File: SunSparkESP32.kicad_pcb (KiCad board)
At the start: 4 copper layers, 38.1 x 58.2 mm, 50 parts, among them J1 Conn_01x02_Pin, J2 USB_C_Receptacle_USB2.0, J4 Conn_01x15_Pin, J5 Conn_01x03_Pin, J6 Conn_01x15_Pin, J7 Conn_01x01_Pin, Q1 IRLML6244TRPBF, Q2 IRLML6244TRPBF, SW1 SW_Push, SW2 SW_Push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

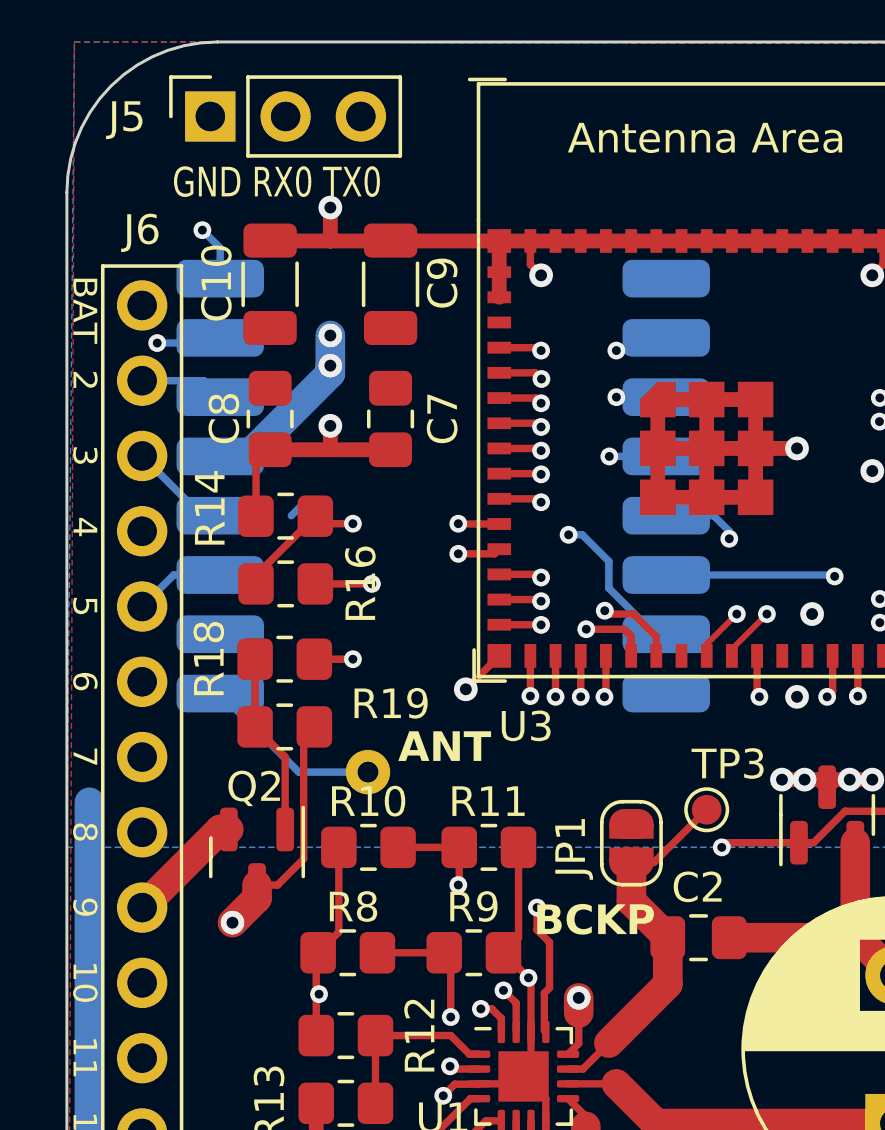
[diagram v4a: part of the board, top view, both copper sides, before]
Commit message: Final adjustments for release preparation -Updated schematics, BOM and fabrication files -Added solder jumper so RFM96 can be powered independently
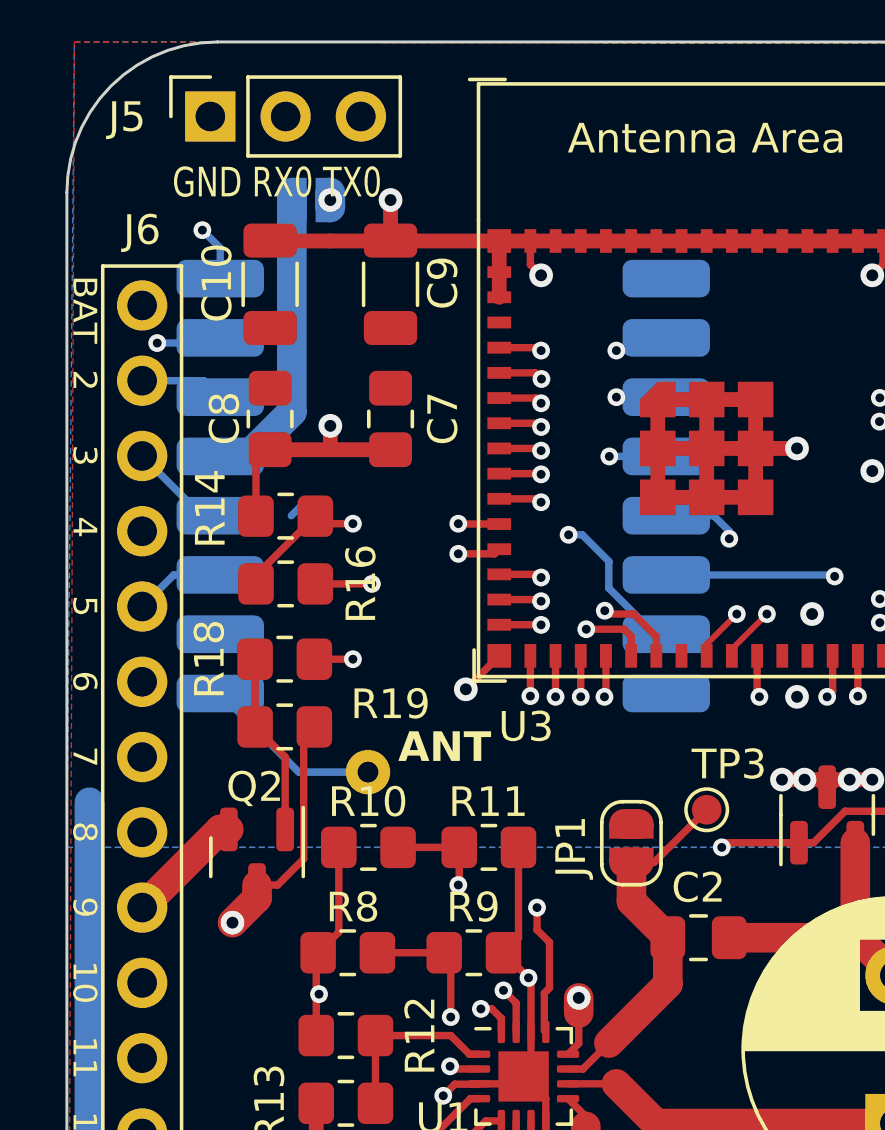
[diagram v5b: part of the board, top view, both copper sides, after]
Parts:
- added JP2: SolderJumper_2_Open, Jumper:SolderJumper-2_P1.3mm_Open_RoundedPad1.0x1.5mm, B.Cu at (60.3, 44.7)
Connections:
- U4 pad 13: +BATT -> Net-(JP2-A)
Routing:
- net Net-(JP2-A): track 0.00 -> 10.2 mm
- net +BATT: track 13.3 -> 7.10 mm, vias 6 -> 5
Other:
- board text removed: "BCKP"
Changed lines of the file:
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@@
   (net 64 "R_DIV_SUPPLY")
   (net 65 "Net-(U1-BAT)")
+  (net 66 "Net-(JP2-A)")
   (footprint "Capacitor_SMD:C_0805_2012Metric_Pad1.18x1.45mm_HandSolder" (layer "F.Cu")
     (at 70.3365 85.598)
@@
       (net 55 "Net-(J7-Pin_1)") (pinfunction "Pin_1") (pintype "passive"))
   )
+  (footprint "Jumper:SolderJumper-2_P1.3mm_Open_RoundedPad1.0x1.5mm" (layer "B.Cu")
+    (at 60.31 44.704)
+    (descr "SMD Solder Jumper, 1x1.5mm, rounded Pads, 0.3mm gap, open")
+    (tags "solder jumper open")
+    (property "Sheetfile" "SunSparkESP32.kicad_sch")
+    (property "Sheetname" "")
+    (property "ki_description" "Solder Jumper, 2-pole, open")
+    (property "ki_keywords" "solder jumper SPST")
+    (attr exclude_from_pos_files)
+    (fp_text reference "JP2" (at -2.906 -0.508) (layer "B.SilkS")
+        (effects (font (size 1 1) (thickness 0.15)) (justify mirror))
+    )
+    (fp_text value "SolderJumper_2_Open" (at 0 -1.9) (layer "B.Fab")
+        (effects (font (size 1 1) (thickness 0.15)) (justify mirror))
+    )
+    (fp_line (start -1.4 -0.3) (end -1.4 0.3)
+      (stroke (width 0.12) (type solid)) (layer "B.SilkS"))
+    (fp_line (start -0.7 1) (end 0.7 1)
+      (stroke (width 0.12) (type solid)) (layer "B.SilkS"))
+    (fp_line (start 0.7 -1) (end -0.7 -1)
+      (stroke (width 0.12) (type solid)) (layer "B.SilkS"))
+    (fp_line (start 1.4 0.3) (end 1.4 -0.3)
+      (stroke (width 0.12) (type solid)) (layer "B.SilkS"))
+    (fp_arc (start -1.4 -0.3) (mid -1.194975 -0.794975) (end -0.7 -1)
+      (stroke (width 0.12) (type solid)) (layer "B.SilkS"))
+    (fp_arc (start -0.7 1) (mid -1.194975 0.794975) (end -1.4 0.3)
+      (stroke (width 0.12) (type solid)) (layer "B.SilkS"))
+    (fp_arc (start 0.7 -1) (mid 1.194975 -0.794975) (end 1.4 -0.3)
+      (stroke (width 0.12) (type solid)) (layer "B.SilkS"))
+    (fp_arc (start 1.4 0.3) (mid 1.194975 0.794975) (end 0.7 1)
+      (stroke (width 0.12) (type solid)) (layer "B.SilkS"))
+    (fp_line (start -1.65 1.25) (end -1.65 -1.25)
+      (stroke (width 0.05) (type solid)) (layer "B.CrtYd"))
+    (fp_line (start -1.65 1.25) (end 1.65 1.25)
+      (stroke (width 0.05) (type solid)) (layer "B.CrtYd"))
+    (fp_line (start 1.65 -1.25) (end -1.65 -1.25)
+      (stroke (width 0.05) (type solid)) (layer "B.CrtYd"))
+    (fp_line (start 1.65 -1.25) (end 1.65 1.25)
+      (stroke (width 0.05) (type solid)) (layer "B.CrtYd"))
+    (pad "1" smd custom (at -0.65 0) (size 1 0.5) (layers "B.Cu" "B.Mask")
+      (net 66 "Net-(JP2-A)") (pinfunction "A") (pintype "passive") (zone_connect 2) (thermal_bridge_angle 45)
+      (options (clearance outline) (anchor rect))
+      (primitives
+        (gr_circle (center 0 -0.25) (end 0.5 -0.25) (width 0) (fill yes))
+        (gr_circle (center 0 0.25) (end 0.5 0.25) (width 0) (fill yes))
+        (gr_poly
+          (pts
+            (xy 0.5 -0.75)
+            (xy 0 -0.75)
+            (xy 0 0.75)
+            (xy 0.5 0.75)
+          )
+          (width 0) (fill yes))
+      ))
+    (pad "2" smd custom (at 0.65 0) (size 1 0.5) (layers "B.Cu" "B.Mask")
+      (net 5 "+BATT") (pinfunction "B") (pintype "passive") (zone_connect 2) (thermal_bridge_angle 45)
+      (options (clearance outline) (anchor rect))
+      (primitives
+        (gr_circle (center 0 -0.25) (end 0.5 -0.25) (width 0) (fill yes))
+        (gr_circle (center 0 0.25) (end 0.5 0.25) (width 0) (fill yes))
+        (gr_poly
+          (pts
+            (xy 0 -0.75)
+            (xy -0.5 -0.75)
+            (xy -0.5 0.75)
+            (xy 0 0.75)
+          )
+          (width 0) (fill yes))
+      ))
+  )
   (footprint "RF_Module:HOPERF_RFM9XW_SMD" (layer "B.Cu")
     (at 64.77 54.356 180)
@@
       (net 9 "/DIO4") (pinfunction "DIO4") (pintype "bidirectional"))
     (pad "13" smd roundrect (at 7.525 1 180) (size 2.95 1.27) (layers "B.Cu" "B.Paste" "B.Mask") (roundrect_rratio 0.25)
-      (net 5 "+BATT") (pinfunction "3.3V") (pintype "power_in"))
+      (net 66 "Net-(JP2-A)") (pinfunction "3.3V") (pintype "power_in"))
     (pad "14" smd roundrect (at 7.525 3 180) (size 2.95 1.27) (layers "B.Cu" "B.Paste" "B.Mask") (roundrect_rratio 0.25)
       (net 10 "/DIO0") (pinfunction "DIO0") (pintype "bidirectional"))
@@
     (effects (font (size 0.8 0.85) (thickness 0.15)) (justify left bottom))
   )
-  (gr_text "BCKP" (at 67.818 69.596) (layer "F.SilkS")
-    (effects (font (size 1 1) (thickness 0.2125) bold) (justify left bottom))
-  )
   (gr_text "35" (at 90.043 59.436 90) (layer "F.SilkS")
     (effects (font (size 0.8 1) (thickness 0.15)) (justify left bottom))
@@
   (segment (start 88.416 94.802) (end 80.716 94.802) (width 1) (layer "F.Cu") (net 4))
   (via (at 77.216 58.674) (size 0.8) (drill 0.4) (layers "F.Cu" "B.Cu") (free) (net 5))
-  (via (at 60.96 50.292) (size 0.8) (drill 0.4) (layers "F.Cu" "B.Cu") (net 5))
-  (via (at 60.96 49.276) (size 0.8) (drill 0.4) (layers "F.Cu" "B.Cu") (net 5))
+  (via (at 60.96 44.704) (size 0.8) (drill 0.4) (layers "F.Cu" "B.Cu") (net 5))
   (via (at 76.708 61.468) (size 0.8) (drill 0.4) (layers "F.Cu" "B.Cu") (free) (net 5))
   (via (at 82.296 51.308) (size 0.8) (drill 0.4) (layers "F.Cu" "B.Cu") (free) (net 5))
@@
   (segment (start 82.296 51.308) (end 81.788 51.308) (width 0.5) (layer "In2.Cu") (net 5))
   (segment (start 81.788 51.308) (end 79.248 53.848) (width 0.5) (layer "In2.Cu") (net 5))
-  (segment (start 60.96 50.292) (end 60.96 50.554962) (width 1) (layer "B.Cu") (net 5))
-  (segment (start 60.96 49.276) (end 60.96 50.292) (width 1) (layer "B.Cu") (net 5))
-  (segment (start 60.96 50.554962) (end 58.158962 53.356) (width 1) (layer "B.Cu") (net 5))
-  (segment (start 58.158962 53.356) (end 57.245 53.356) (width 1) (layer "B.Cu") (net 5))
   (segment (start 69.596 59.186498) (end 70.870498 59.186498) (width 0.25) (layer "F.Cu") (net 6))
   (segment (start 70.870498 59.186498) (end 71.11 59.426) (width 0.25) (layer "F.Cu") (net 6))
@@
   (segment (start 55.372 96.331) (end 54.422 95.381) (width 0.5) (layer "F.Cu") (net 47))
   (segment (start 88.172 47.718) (end 87.63 48.26) (width 0.25) (layer "F.Cu") (net 47))
+  (segment (start 62.992 44.704) (end 62.992 46.072) (width 0.5) (layer "F.Cu") (net 47))
   (segment (start 80.66 48.836) (end 80.66 49.686) (width 0.25) (layer "F.Cu") (net 47))
   (segment (start 79.61 46.086) (end 79.61 46.882) (width 0.25) (layer "F.Cu") (net 47))
@@
   (segment (start 87.122 41.402) (end 87.122 41.851327) (width 0.25) (layer "F.Cu") (net 47))
   (segment (start 54.422 95.381) (end 54.422 84.008) (width 0.5) (layer "F.Cu") (net 47))
-  (segment (start 60.96 44.958) (end 60.96 46.086) (width 0.5) (layer "F.Cu") (net 47))
   (via (at 79.248 47.244) (size 0.8) (drill 0.4) (layers "F.Cu" "B.Cu") (net 47))
   (via (at 65.532 61.214) (size 0.8) (drill 0.4) (layers "F.Cu" "B.Cu") (net 47))
@@
   (via (at 76.2 64.262) (size 0.8) (drill 0.4) (layers "F.Cu" "B.Cu") (net 47))
   (via (at 76.708 53.086) (size 0.8) (drill 0.4) (layers "F.Cu" "B.Cu") (net 47))
-  (via (at 60.96 44.958) (size 0.8) (drill 0.4) (layers "F.Cu" "B.Cu") (net 47))
+  (via (at 62.992 44.704) (size 0.8) (drill 0.4) (layers "F.Cu" "B.Cu") (net 47))
   (via (at 80.66 61.468) (size 0.8) (drill 0.4) (layers "F.Cu" "B.Cu") (net 47))
   (via (at 68.072 47.244) (size 0.8) (drill 0.4) (layers "F.Cu" "B.Cu") (net 47))
@@
   (segment (start 80.01 75.866) (end 71.951 75.866) (width 1) (layer "F.Cu") (net 65))
   (segment (start 70.612 74.527) (end 68.981 74.527) (width 0.25) (layer "F.Cu") (net 65))
+  (segment (start 57.245 53.356) (end 58.158962 53.356) (width 1) (layer "B.Cu") (net 66))
+  (segment (start 58.158962 53.356) (end 59.66 51.854962) (width 1) (layer "B.Cu") (net 66))
+  (segment (start 59.66 51.854962) (end 59.66 44.704) (width 1) (layer "B.Cu") (net 66))
   (zone (net 5) (net_name "+BATT") (layer "F.Cu") (hatch edge 0.5)
     (priority 1)

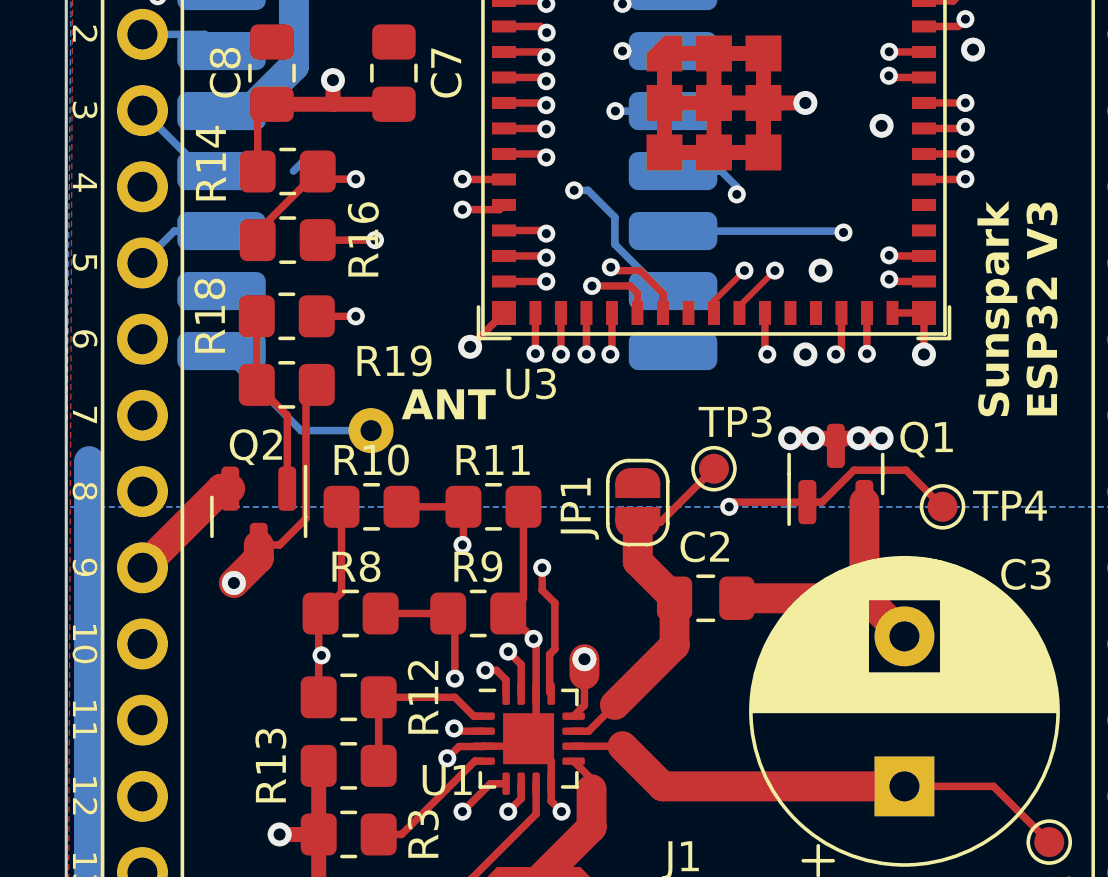
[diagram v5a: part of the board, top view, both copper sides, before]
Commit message: connected RF96 pin to µC instead of reset button
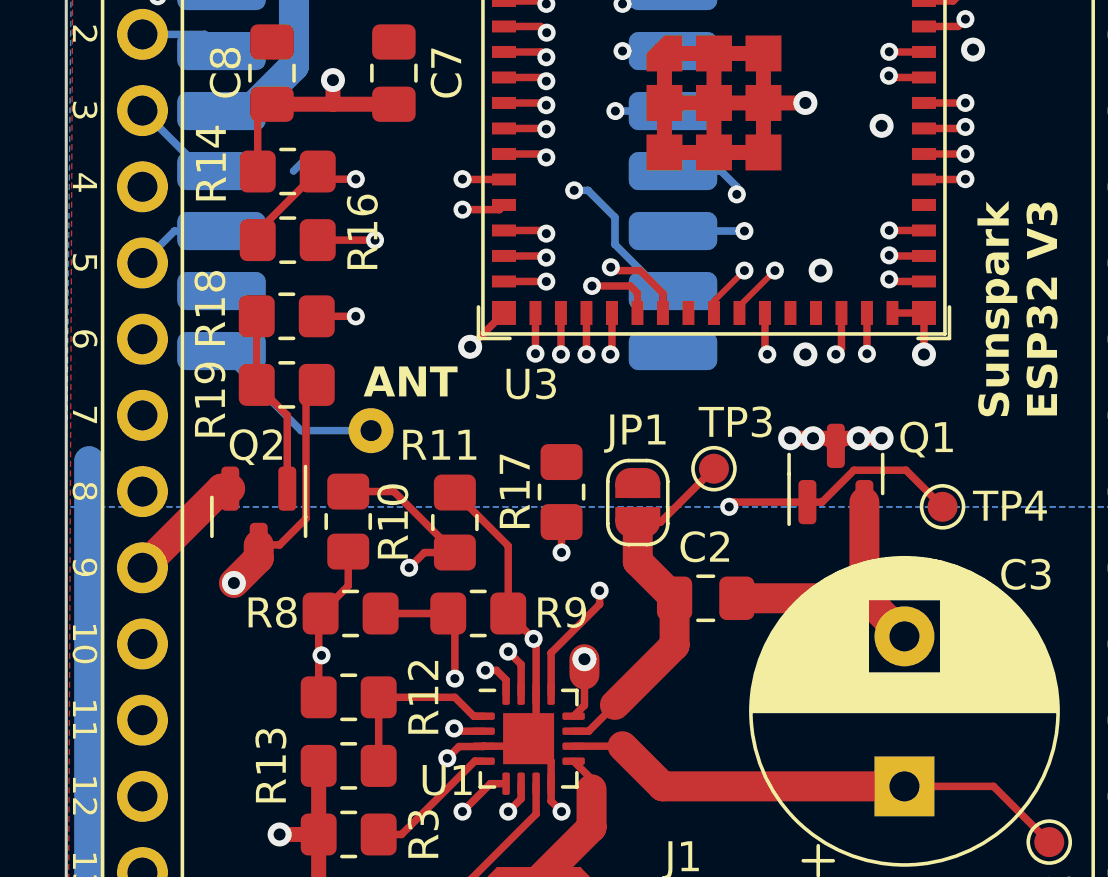
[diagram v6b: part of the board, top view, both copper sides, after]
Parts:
- added R17: 10k, Resistor_SMD:R_0805_2012Metric_Pad1.20x1.40mm_HandSolder, F.Cu at (68.6, 66.1)
- moved R11 1.39 mm to (65.0, 67.1), turned to 90 degrees
- moved R10 0.92 mm to (61.5, 67.0), turned to 90 degrees
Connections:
- U3 pad 33: unconnected-(U3-GPIO37-Pad33) -> /RF96_RST
- U4 pad 6: rst_btn -> /RF96_RST
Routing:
- net /RF96_RST: track 0.00 -> 22.6 mm, vias 0 -> 3
- net rst_btn: track 83.1 -> 65.3 mm, vias 4 -> 3
- net Net-(U1-SETPG): track 9.13 -> 11.9 mm
- net PGOOD: track 19.7 -> 17.7 mm
- net Net-(U1-REF): track 14.5 -> 13.1 mm
- net GND: track 70.2 -> 71.2 mm
